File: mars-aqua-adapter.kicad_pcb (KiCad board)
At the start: 2 copper layers, 35.7 x 37.2 mm, 38 parts, among them J1 Conn_01x03, J2 Conn_01x03, J3 Conn_01x04, J4 Conn_01x04, Q1 PNP, Q2 PNP, U1 LM358, U2 LM393

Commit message: board layout
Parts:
- added J5: Conn_01x03, Connector_PinHeader_2.54mm:PinHeader_1x03_P2.54mm_Vertical, F.Cu at (111.9, 96.9)
- added J6: Conn_01x03, Connector_PinHeader_2.54mm:PinHeader_1x03_P2.54mm_Vertical, F.Cu at (111.8, 87.3)
- added R19: 100k, Resistor_SMD:R_0603_1608Metric_Pad1.05x0.95mm_HandSolder, F.Cu at (122.3, 87.2)
- added R20: 100k, Resistor_SMD:R_0603_1608Metric_Pad1.05x0.95mm_HandSolder, F.Cu at (124.0, 102.8)
- added REF**: MountingHole_3.2mm_M3, MountingHole:MountingHole_3.2mm_M3, F.Cu at (110.6, 80.6)
- added REF**: MountingHole_3.2mm_M3, MountingHole:MountingHole_3.2mm_M3, F.Cu at (110.6, 110.0)
- added REF**: MountingHole_3.2mm_M3, MountingHole:MountingHole_3.2mm_M3, F.Cu at (153.1, 110.0)
- added REF**: MountingHole_3.2mm_M3, MountingHole:MountingHole_3.2mm_M3, F.Cu at (153.1, 80.6)
- Q1, Q2: value PNP -> Q_PNP_BEC
- R7, R8: value 330k -> 100k
- moved D2 6.36 mm to (127.7, 109.8), turned to 90 degrees
- moved REF** 5.19 mm to (150.7, 94.7)
- moved R14 5.01 mm to (135.3, 102.8)
- moved R8 1.99 mm to (125.7, 102.8)
- moved R13 1.91 mm to (133.7, 102.8)
- moved VR2 1.64 mm to (131.6, 109.4), turned to 90 degrees
- moved R10 1.38 mm to (131.9, 102.8)
- moved C4 1.05 mm to (127.7, 102.8)
- moved C3 0.68 mm to (120.2, 102.8)
- moved C1 0.65 mm to (127.7, 87.2)
- moved R7 0.60 mm to (125.7, 87.2)
- moved R6 0.60 mm to (122.3, 102.8)
- moved J2 0.60 mm to (123.2, 110.2)
- moved R5 0.43 mm to (124.0, 87.2)
- moved C2 0.32 mm to (120.2, 87.2)
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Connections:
- Q1 pad 1: +12V -> Net-(Q1-Pad1)
- Q1 pad 2: Net-(Q1-Pad2) -> +12V
- Q2 pad 1: +12V -> Net-(Q2-Pad1)
- Q2 pad 2: Net-(Q2-Pad2) -> +12V
- R17 pad 1: Net-(Q1-Pad2) -> Net-(Q1-Pad1)
- R18 pad 1: Net-(Q2-Pad2) -> Net-(Q2-Pad1)
- R5 pad 1: Net-(R5-Pad1) -> Net-(J6-Pad3)
- R6 pad 1: Net-(R6-Pad1) -> Net-(J5-Pad3)
- R7 pad 1: /ch1_output -> Net-(J6-Pad2)
- R7 pad 2: Net-(R5-Pad1) -> /ch1_output
- R8 pad 1: /ch2_output -> Net-(J5-Pad2)
- R8 pad 2: Net-(R6-Pad1) -> /ch2_output
- U1 pad 2: Net-(R5-Pad1) -> Net-(J6-Pad3)
- U1 pad 6: Net-(R6-Pad1) -> Net-(J5-Pad3)
- U2 pad 4: +12V -> (no net)
- U2 pad 8: GND -> (no net)
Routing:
- net Net-(J6-Pad3): track 0.00 -> 22.7 mm, vias 0 -> 2
- net Net-(J5-Pad2): track 0.00 -> 21.7 mm, vias 0 -> 2
- net Net-(J5-Pad3): track 0.00 -> 20.3 mm
- net Net-(J5-Pad1): track 0.00 -> 19.3 mm, vias 0 -> 2
- net Net-(J6-Pad2): track 0.00 -> 18.8 mm, vias 0 -> 2
- net Net-(J6-Pad1): track 0.00 -> 15.6 mm, vias 0 -> 2
- net /ch1_input: track 52.4 -> 42.0 mm, vias 2 -> 1
- net /ch2_input: track 40.5 -> 50.0 mm, vias 0 -> 2
- net Net-(Q2-Pad2): track 8.47 -> 0.00 mm
- net Net-(Q2-Pad1): track 0.00 -> 8.23 mm
- net Net-(R5-Pad1): track 6.42 -> 0.00 mm
- net Net-(R6-Pad1): track 6.24 -> 0.00 mm
- net +12V: track 39.6 -> 35.1 mm, vias 7 -> 5
- net Net-(R13-Pad1): track 8.80 -> 4.86 mm
- net /ch1_output: track 38.7 -> 35.0 mm
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- added copper zone on B.Cu, net GND
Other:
- board size 35.7 x 37.2 mm -> 50.7 x 37.2 mm
- board text added: "3.3v"
- board text added: "5v"
- board text added: "pwm input config"

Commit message: Final Layout
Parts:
- C1, C4: footprint Capacitor_SMD:C_1206_3216Metric_Pad1.42x1.75mm_HandSolder -> Capacitor_SMD:C_0805_2012Metric
- C2, C3: value 0.1uF -> 4.7uF; footprint Capacitor_SMD:C_1206_3216Metric_Pad1.42x1.75mm_HandSolder -> Capacitor_SMD:C_0805_2012Metric
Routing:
- net +12V: track 35.1 -> 37.0 mm

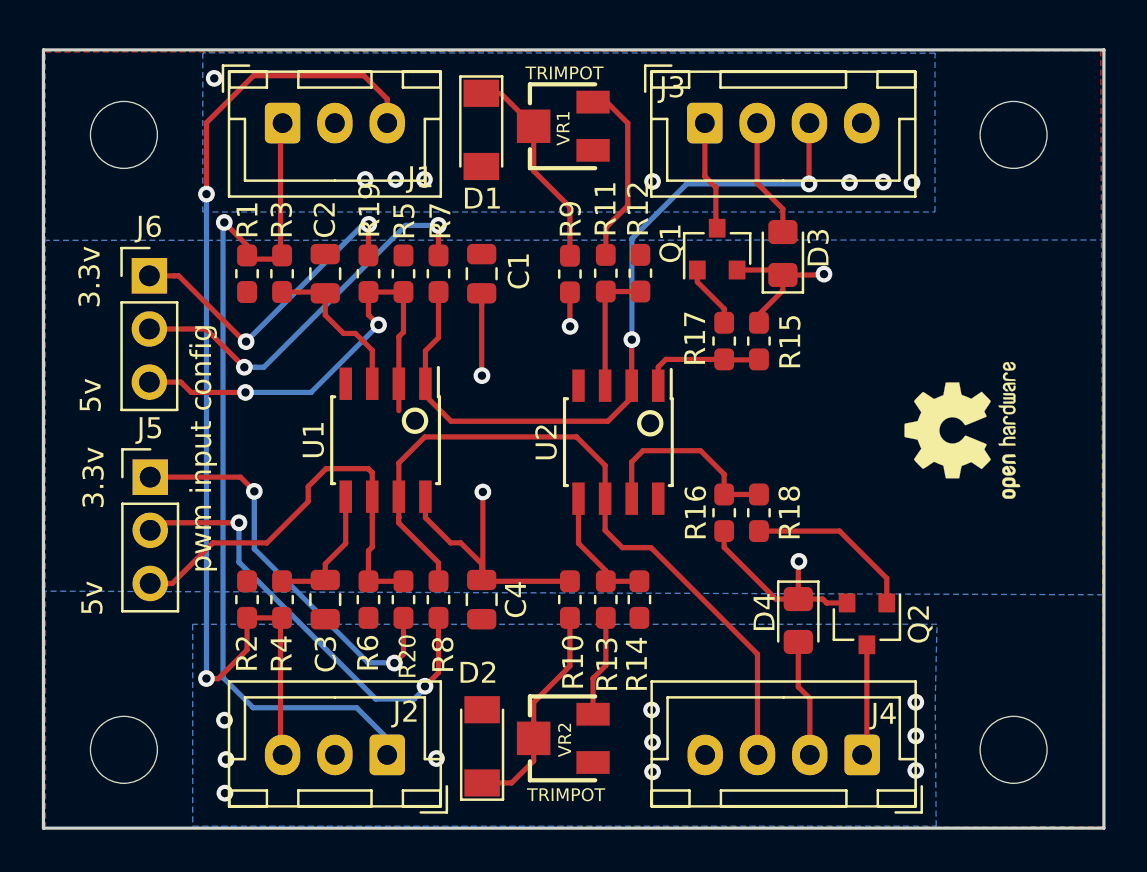
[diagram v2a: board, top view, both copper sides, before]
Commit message: Fix traces on comparator
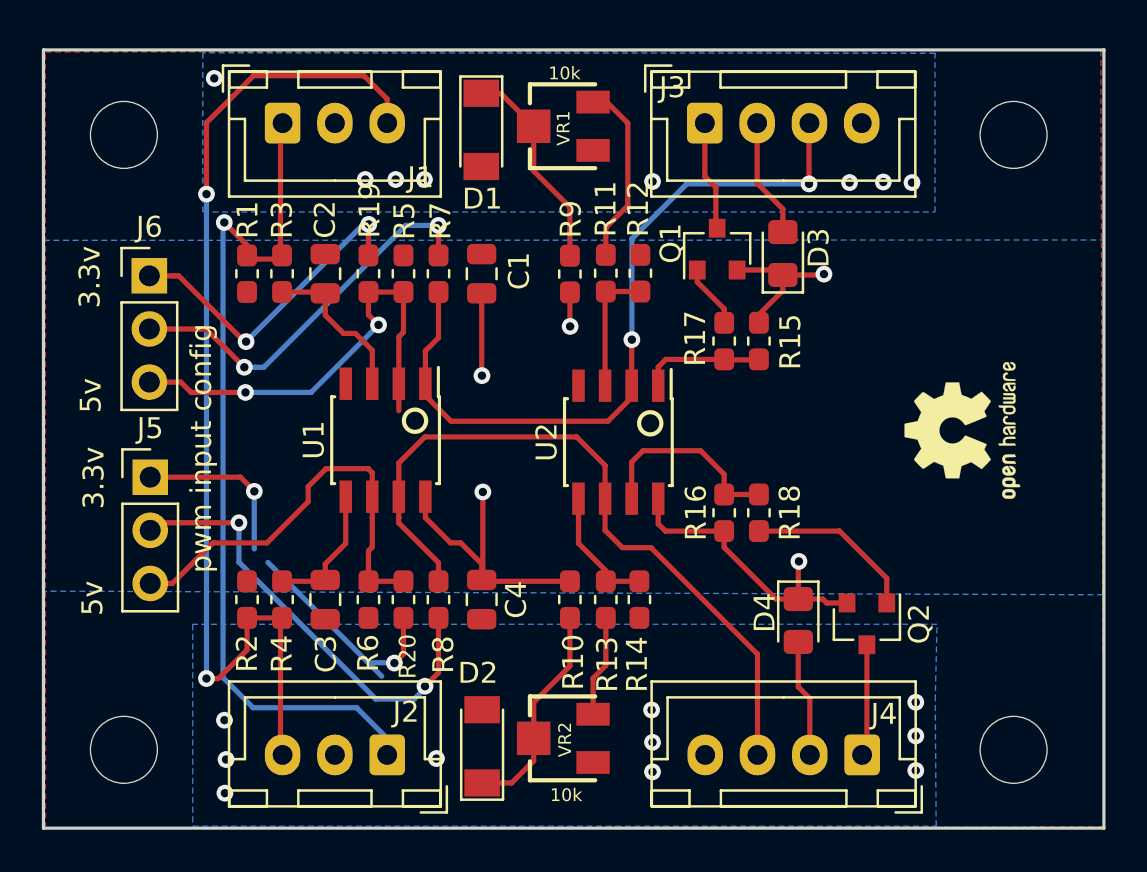
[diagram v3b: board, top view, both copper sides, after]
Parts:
- R11, R13: value 30k -> 39k
- R12, R14: value 10k -> 20k
- VR1, VR2: value TRIMPOT -> 10k
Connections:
- U2 pad 4: (no net) -> GND
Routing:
- net +12V: track 37.0 -> 41.5 mm
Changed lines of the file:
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@@
     (thickness 1.6)
     (drawings 12)
-    (tracks 266)
+    (tracks 269)
     (zones 0)
     (modules 46)
@@
     (pad 5 smd rect (at 2.7 1.905 270) (size 1.55 0.6) (layers F.Cu F.Paste F.Mask)
       (net 16 "Net-(R13-Pad2)"))
-    (pad 4 smd rect (at -2.7 1.905 270) (size 1.55 0.6) (layers F.Cu F.Paste F.Mask))
+    (pad 4 smd rect (at -2.7 1.905 270) (size 1.55 0.6) (layers F.Cu F.Paste F.SilkS F.Mask)
+      (net 2 GND))
     (pad 3 smd rect (at -2.7 0.635 270) (size 1.55 0.6) (layers F.Cu F.Paste F.Mask)
       (net 13 "Net-(R11-Pad2)"))
@@
       (effects (font (size 1 1) (thickness 0.15)))
     )
-    (fp_text value 30k (at 2.88324 0.18062 90) (layer F.Fab)
+    (fp_text value 39k (at 2.88324 0.18062 90) (layer F.Fab)
       (effects (font (size 1 1) (thickness 0.15)))
     )
@@
       (effects (font (size 1 1) (thickness 0.15)))
     )
-    (fp_text value 10k (at 0 1.43 90) (layer F.Fab)
+    (fp_text value 20k (at 0 1.43 90) (layer F.Fab)
       (effects (font (size 1 1) (thickness 0.15)))
     )
@@
       (effects (font (size 1 1) (thickness 0.15)))
     )
-    (fp_text value 30k (at -3.075 0.1 90) (layer F.Fab)
+    (fp_text value 39k (at -3.075 0.1 90) (layer F.Fab)
       (effects (font (size 1 1) (thickness 0.15)))
     )
@@
       (effects (font (size 1 1) (thickness 0.15)))
     )
-    (fp_text value 10k (at 3.025 0 270) (layer F.Fab)
+    (fp_text value 20k (at 3.025 0 270) (layer F.Fab)
       (effects (font (size 1 1) (thickness 0.15)))
     )
@@
       (effects (font (size 0.6096 0.6096) (thickness 0.127)))
     )
-    (fp_text value TRIMPOT (at 2.5276 0.05374 180) (layer F.SilkS)
+    (fp_text value 10k (at 2.5276 0.05374 180) (layer F.SilkS)
       (effects (font (size 0.6096 0.6096) (thickness 0.127)))
     )
@@
       (effects (font (size 0.6096 0.6096) (thickness 0.127)))
     )
-    (fp_text value TRIMPOT (at -2.71526 0.13248) (layer F.SilkS)
+    (fp_text value 10k (at -2.71526 0.13248) (layer F.SilkS)
       (effects (font (size 0.6096 0.6096) (thickness 0.127)))
     )
@@
   (segment (start 127.77216 101.78162) (end 127.71628 101.8375) (width 0.25) (layer F.Cu) (net 1))
   (segment (start 127.77216 97.63252) (end 127.77216 101.78162) (width 0.25) (layer F.Cu) (net 1))
+  (segment (start 136.155 97.95) (end 136.155 99.155) (width 0.25) (layer F.Cu) (net 1))
+  (segment (start 136.5 99.5) (end 139.3063 99.5) (width 0.25) (layer F.Cu) (net 1))
+  (segment (start 136.155 99.155) (end 136.5 99.5) (width 0.25) (layer F.Cu) (net 1))
   (segment (start 127.65 81.95) (end 128.4 81.95) (width 0.25) (layer F.Cu) (net 2))
   (segment (start 127.9 82.2) (end 128.15 82.2) (width 0.25) (layer F.Cu) (net 2))
@@
   (segment (start 123.52782 105.79354) (end 122.2883 105.79354) (width 0.25) (layer B.Cu) (net 23))
   (segment (start 123.54306 105.80878) (end 123.52782 105.79354) (width 0.25) (layer B.Cu) (net 23))
-  (segment (start 122.2883 105.79354) (end 116.84762 100.35286) (width 0.25) (layer B.Cu) (net 23))
+  (segment (start 122.94068 106.44068) (end 117.5 101) (width 0.25) (layer B.Cu) (net 23))
   (segment (start 123.97752 105.37432) (end 123.54306 105.80878) (width 0.25) (layer F.Cu) (net 23))
   (segment (start 123.97752 103.65) (end 123.97752 105.37432) (width 0.25) (layer F.Cu) (net 23))

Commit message: Add hysteresis
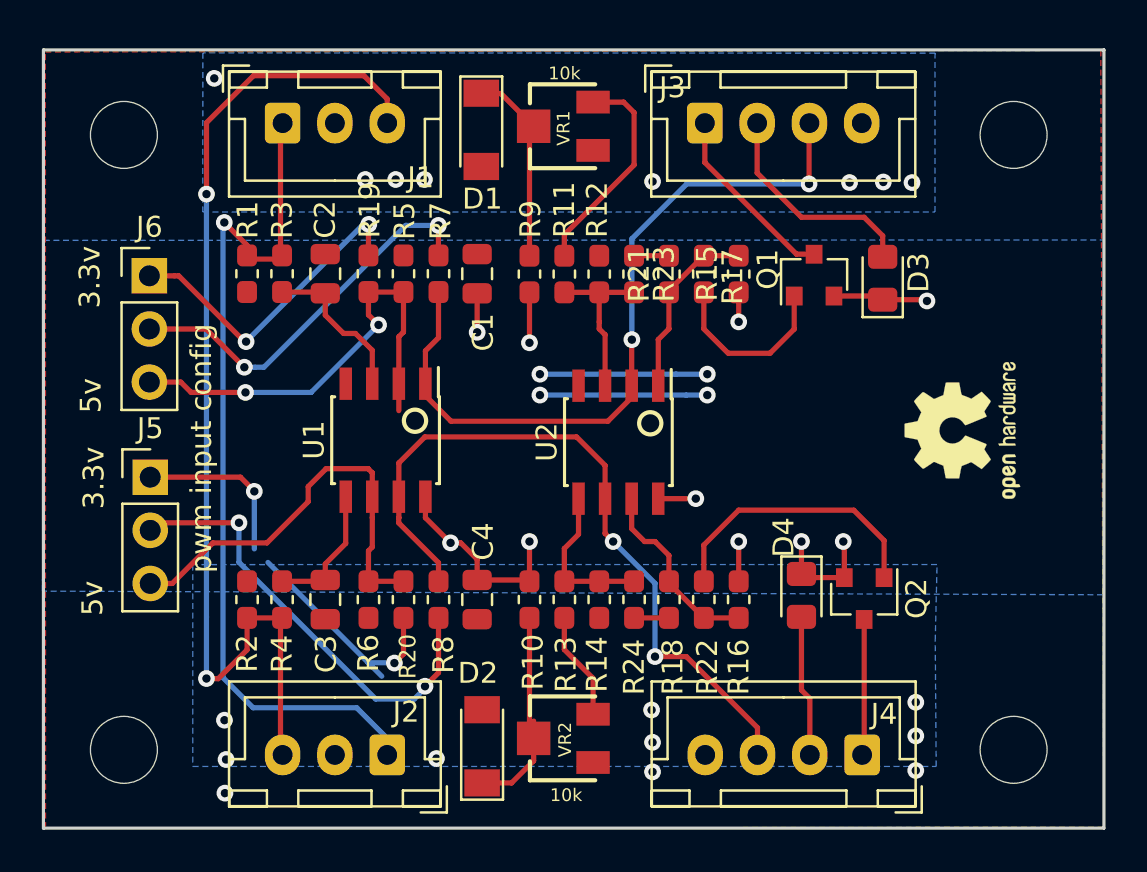
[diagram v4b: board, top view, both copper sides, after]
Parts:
- added R21: 1M, Resistor_SMD:R_0603_1608Metric_Pad1.05x0.95mm_HandSolder, F.Cu at (136.7, 87.2)
- added R22: 1M, Resistor_SMD:R_0603_1608Metric_Pad1.05x0.95mm_HandSolder, F.Cu at (136.7, 102.8)
- added R23: 1M, Resistor_SMD:R_0603_1608Metric_Pad1.05x0.95mm_HandSolder, F.Cu at (135.0, 87.2)
- added R24: 1M, Resistor_SMD:R_0603_1608Metric_Pad1.05x0.95mm_HandSolder, F.Cu at (135.0, 102.8)
- moved R18 4.92 mm to (138.3, 102.8), turned to 270 degrees
- moved D3 4.91 mm to (146.9, 87.4)
- moved Q1 4.80 mm to (143.6, 87.3)
- moved R16 4.21 mm to (140.0, 102.8), turned to 270 degrees
- moved R17 3.35 mm to (138.3, 87.2), turned to 90 degrees
- moved R15 3.35 mm to (140.0, 87.2), turned to 90 degrees
- moved R11 1.98 mm to (131.7, 87.2)
- moved R13 1.98 mm to (131.7, 102.8)
- moved R12 1.97 mm to (133.3, 87.2)
- moved R10 1.93 mm to (130.0, 102.8)
- moved R9 1.93 mm to (130.0, 87.2)
- moved R14 1.92 mm to (133.3, 102.8)
- moved Q2 1.22 mm to (146.0, 102.7)
- moved D4 1.21 mm to (143.0, 102.6)
- moved C1 0.22 mm to (127.5, 87.2)
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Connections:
- U2 pad 8: (no net) -> +12V
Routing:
- net GND: track 1.00 -> 17.0 mm, vias 18 -> 22
- net +12V: track 41.5 -> 29.7 mm, vias 5 -> 10
- net Net-(Q1-Pad1): track 3.05 -> 8.61 mm
- net Net-(Q2-Pad1): track 8.23 -> 13.4 mm
- net Net-(D3-Pad2): track 5.72 -> 10.6 mm
- net /ch1_enable: track 5.27 -> 8.92 mm
- net Net-(R15-Pad2): track 5.87 -> 8.78 mm
- net Net-(R11-Pad2): track 6.16 -> 7.91 mm
- net Net-(R22-Pad2): track 0.00 -> 1.67 mm
- net Net-(R21-Pad2): track 0.00 -> 1.67 mm
- net Net-(R11-Pad1): track 8.81 -> 10.4 mm
- net Net-(R13-Pad2): track 6.10 -> 7.56 mm
- net /ch2_enable: track 5.71 -> 6.87 mm
- net Net-(D4-Pad2): track 5.63 -> 6.77 mm
- net Net-(D2-Pad1): track 11.4 -> 10.7 mm
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
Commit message: Add voltage reference
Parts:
- removed D2: 3v3, Diode_SMD:D_MiniMELF
- removed the R20 at (124.0, 102.8)
- removed the R6 at (122.3, 102.8)
- removed the R8 at (125.7, 102.8)
- removed the REF** at (110.6, 80.6)
- removed the REF** at (110.6, 110.0)
- removed the REF** at (153.1, 110.0)
- removed the REF** at (153.1, 80.6)
- removed VR1, VR2: 10k, Resistors:TRIMPOT-SMD-3MM-OPEN
- added C5: 10nF, Capacitor_SMD:C_0603_1608Metric, F.Cu at (145.5, 98.6)
- added Q3: Q_NPN_BEC, Package_TO_SOT_SMD:SOT-23, F.Cu at (153.3, 87.7)
- added Q4: Q_NPN_BEC, Package_TO_SOT_SMD:SOT-23, F.Cu at (153.3, 102.3)
- added R1: 330k, Resistor_SMD:R_0603_1608Metric_Pad1.05x0.95mm_HandSolder, F.Cu at (116.5, 102.3)
- added R11: 100k, Resistor_SMD:R_0603_1608Metric_Pad1.05x0.95mm_HandSolder, F.Cu at (137.9, 102.3)
- added R12: 1M, Resistor_SMD:R_0603_1608Metric_Pad1.05x0.95mm_HandSolder, F.Cu at (139.6, 102.3)
- added R13: 100k, Resistor_SMD:R_0603_1608Metric_Pad1.05x0.95mm_HandSolder, F.Cu at (149.9, 102.3)
- added R25: 1M, Resistor_SMD:R_0603_1608Metric_Pad1.05x0.95mm_HandSolder, F.Cu at (139.6, 87.7)
- added R26: 100k, Resistor_SMD:R_0603_1608Metric_Pad1.05x0.95mm_HandSolder, F.Cu at (149.9, 87.7)
- added R3: 100k, Resistor_SMD:R_0603_1608Metric_Pad1.05x0.95mm_HandSolder, F.Cu at (122.3, 102.3)
- added R5: 100k, Resistor_SMD:R_0603_1608Metric_Pad1.05x0.95mm_HandSolder, F.Cu at (125.7, 102.3)
- added REF**: MountingHole_3.2mm_M3, MountingHole:MountingHole_3.2mm_M3, F.Cu at (153.7, 110.2)
- added REF**: MountingHole_3.2mm_M3, MountingHole:MountingHole_3.2mm_M3, F.Cu at (110.2, 80.0)
- added REF**: MountingHole_3.2mm_M3, MountingHole:MountingHole_3.2mm_M3, F.Cu at (110.2, 110.2)
- added REF**: MountingHole_3.2mm_M3, MountingHole:MountingHole_3.2mm_M3, F.Cu at (153.7, 80.0)
- C1: value 0.1uF -> 4.7uF; footprint Capacitor_SMD:C_0805_2012Metric -> Capacitor_SMD:C_0603_1608Metric
- C2, C4: footprint Capacitor_SMD:C_0805_2012Metric -> Capacitor_SMD:C_0603_1608Metric
- C3: value 4.7uF -> 0.1uF; footprint Capacitor_SMD:C_0805_2012Metric -> Capacitor_SMD:C_0603_1608Metric
- D1: value 3v3 -> TL431DBZ; footprint Diode_SMD:D_MiniMELF -> Package_TO_SOT_SMD:SOT-23
- R10: renamed from R16; value 18k -> 10k
- R19: renamed from R18; value 10k -> 100k
- R2: value 330k -> 20k
- R21: renamed from R15; value 18k -> 10k
- R22: renamed from R11; value 39k -> 330k
- R23: renamed from R12; value 20k -> 82k
- R24: value 1M -> 100k
- R27: renamed from R17; value 10k -> 100k
- R28: renamed from R10; value 10k -> 100k
- R29: renamed from R9; value 10k -> 22
- R4: value 20k -> 100k
- R6: renamed from R23; value 1M -> 100k
- R8: renamed from R14; value 20k -> 82k
- R9: renamed from R13; value 39k -> 330k
- REF**: value OSHW -> OSHW-Logo2_7.3x6mm_SilkScreen
- moved D1 20.5 mm to (141.7, 95.2), turned to 180 degrees
- moved R29 18.4 mm to (145.5, 97.0), turned to 180 degrees
- moved R19 17.5 mm to (129.5, 87.7)
- moved R28 17.3 mm to (145.5, 95.2), turned to 0 degrees
- moved C1 16.7 mm to (120.2, 102.3), turned to 270 degrees
- moved R6 16.0 mm to (129.5, 102.3), turned to 90 degrees
- moved R24 15.3 mm to (137.9, 87.7)
- moved C4 15.1 mm to (127.5, 87.7), turned to 90 degrees
- moved R27 9.55 mm to (145.5, 93.5), turned to 0 degrees
- moved C3 7.28 mm to (127.5, 102.3)
- moved R21 7.17 mm to (132.8, 87.7), turned to 270 degrees
- moved R4 5.83 mm to (124.0, 102.3), turned to 90 degrees
- moved R7 5.54 mm to (131.2, 102.3), turned to 90 degrees
- moved R20 5.53 mm to (131.2, 87.7), turned to 270 degrees
- moved J1 5.11 mm to (123.2, 81.0), turned to 180 degrees
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- renumbered R1 to R14, R3 to R15, R19 to R16, R5 to R17, R7 to R18, R21 to R20, R22 to R7
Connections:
- C1 pad 1: +12V -> Net-(C1-Pad1)
- C3 pad 1: Net-(C3-Pad1) -> +12V
- D1 pad 1: Net-(D1-Pad1) -> /Vref
- D1 pad 2: GND -> Net-(D1-Pad2)
- R10 pad 1: +12V -> /Vref
- R10 pad 2: Net-(R16-Pad2) -> Net-(R10-Pad2)
- R19 pad 1: Net-(Q2-Pad1) -> Net-(R19-Pad1)
- R19 pad 2: Net-(R16-Pad2) -> /ch1_output
- R2 pad 1: /ch2_input -> Net-(C1-Pad1)
- R2 pad 2: GND -> /ch2_input
- R20 pad 1: Net-(R15-Pad2) -> Net-(R20-Pad1)
- R20 pad 2: Net-(R21-Pad2) -> Net-(R19-Pad1)
- R21 pad 1: +12V -> /Vref
- R21 pad 2: Net-(R15-Pad2) -> Net-(R20-Pad1)
- R22 pad 1: Net-(R11-Pad1) -> /Vref
- R22 pad 2: Net-(R11-Pad2) -> Net-(R22-Pad2)
- R23 pad 1: Net-(R11-Pad2) -> Net-(R22-Pad2)
- R24 pad 1: Net-(R22-Pad2) -> Net-(R20-Pad1)
- R24 pad 2: Net-(R13-Pad2) -> Net-(Q3-Pad1)
- R27 pad 1: Net-(Q1-Pad1) -> Net-(D1-Pad2)
- R27 pad 2: Net-(R15-Pad2) -> GND
- R28 pad 1: +12V -> /Vref
- R28 pad 2: Net-(D2-Pad1) -> Net-(D1-Pad2)
- R29 pad 2: Net-(D1-Pad1) -> /Vref
- R4 pad 1: Net-(C3-Pad1) -> Net-(J5-Pad1)
- R4 pad 2: /ch2_input -> Net-(J5-Pad3)
- R6 pad 1: Net-(R21-Pad2) -> Net-(R6-Pad1)
- R6 pad 2: Net-(R11-Pad2) -> /ch2_output
- R7 pad 1: Net-(R16-Pad2) -> Net-(R10-Pad2)
- R7 pad 2: Net-(R22-Pad2) -> Net-(R6-Pad1)
- R8 pad 1: Net-(R13-Pad2) -> Net-(R8-Pad1)
- R9 pad 1: Net-(R13-Pad1) -> /Vref
- R9 pad 2: Net-(R13-Pad2) -> Net-(R8-Pad1)
- U1 pad 5: Net-(C3-Pad1) -> Net-(C1-Pad1)
- U2 pad 1: Net-(R15-Pad2) -> Net-(R20-Pad1)
- U2 pad 2: /ch1_output -> Net-(R22-Pad2)
- U2 pad 3: Net-(R11-Pad2) -> Net-(R19-Pad1)
- U2 pad 5: Net-(R13-Pad2) -> Net-(R6-Pad1)
- U2 pad 6: /ch2_output -> Net-(R8-Pad1)
- U2 pad 7: Net-(R16-Pad2) -> Net-(R10-Pad2)
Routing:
- net /Vref: track 0.00 -> 51.2 mm, vias 0 -> 4
- net Net-(Q4-Pad1): track 0.00 -> 21.0 mm, vias 0 -> 2
- net Net-(R10-Pad2): track 0.00 -> 20.6 mm, vias 0 -> 2
- net Net-(Q3-Pad1): track 0.00 -> 19.8 mm, vias 0 -> 2
- net GND: track 17.0 -> 0.00 mm, vias 22 -> 18
- net Net-(R20-Pad1): track 0.00 -> 12.1 mm, vias 0 -> 2
- net Net-(Q2-Pad1): track 13.4 -> 2.44 mm
- net Net-(D2-Pad1): track 10.7 -> 0.00 mm
- net Net-(R11-Pad1): track 10.4 -> 0.00 mm
- net +12V: track 29.7 -> 19.6 mm, vias 10 -> 7
- net /ch2_input: track 50.0 -> 40.0 mm
- net Net-(D1-Pad1): track 9.36 -> 0.00 mm
- net Net-(R16-Pad2): track 9.09 -> 0.00 mm
- net Net-(R15-Pad2): track 8.78 -> 0.00 mm
- net Net-(R11-Pad2): track 7.91 -> 0.00 mm
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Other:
- board text added: "Mars Aqua Adapter v3 github.com/ranthalion/mars-aqua"
- board text removed: "Mars Aqua Adapter v2 github.com/ranthalion/mars-aqua"

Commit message: gerber updates
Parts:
- D1: value TL431DBZ -> TL432DBZ
- moved Q3 9.52 mm to (143.8, 87.7)
- moved Q1 6.84 mm to (150.4, 87.7)
- moved D3 6.78 mm to (154.0, 87.7)
- moved C5 5.84 mm to (145.5, 92.7)
- moved R27 4.06 mm to (145.5, 97.5)
- moved R26 2.79 mm to (147.1, 87.7)
- moved R29 2.71 mm to (145.5, 94.3)
- moved R28 0.68 mm to (145.5, 95.9)
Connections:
- D1 pad 1: /Vref -> Net-(D1-Pad1)
- D1 pad 2: Net-(D1-Pad2) -> /Vref
- R27 pad 1: Net-(D1-Pad2) -> Net-(D1-Pad1)
- R28 pad 2: Net-(D1-Pad2) -> Net-(D1-Pad1)
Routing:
- net Net-(Q3-Pad1): track 19.8 -> 5.68 mm, vias 2 -> 0
- net Net-(Q1-Pad1): track 11.9 -> 2.44 mm
- net /ch1_enable: track 9.10 -> 16.9 mm
- net Net-(D3-Pad2): track 11.1 -> 17.4 mm
- net Net-(D1-Pad1): track 0.00 -> 5.23 mm
- net Net-(D1-Pad2): track 4.78 -> 0.00 mm
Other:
- board text added: "CH1"
- board text added: "CH2"
